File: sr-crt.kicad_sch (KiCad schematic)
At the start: 15 parts, among them J1 Conn_02x03_Odd_Even, J2 Barrel_Jack_MountingPin, U1 SN65LVDS2DBV, U2 SN65LVDS2DBV, U3 ADuM1200BR

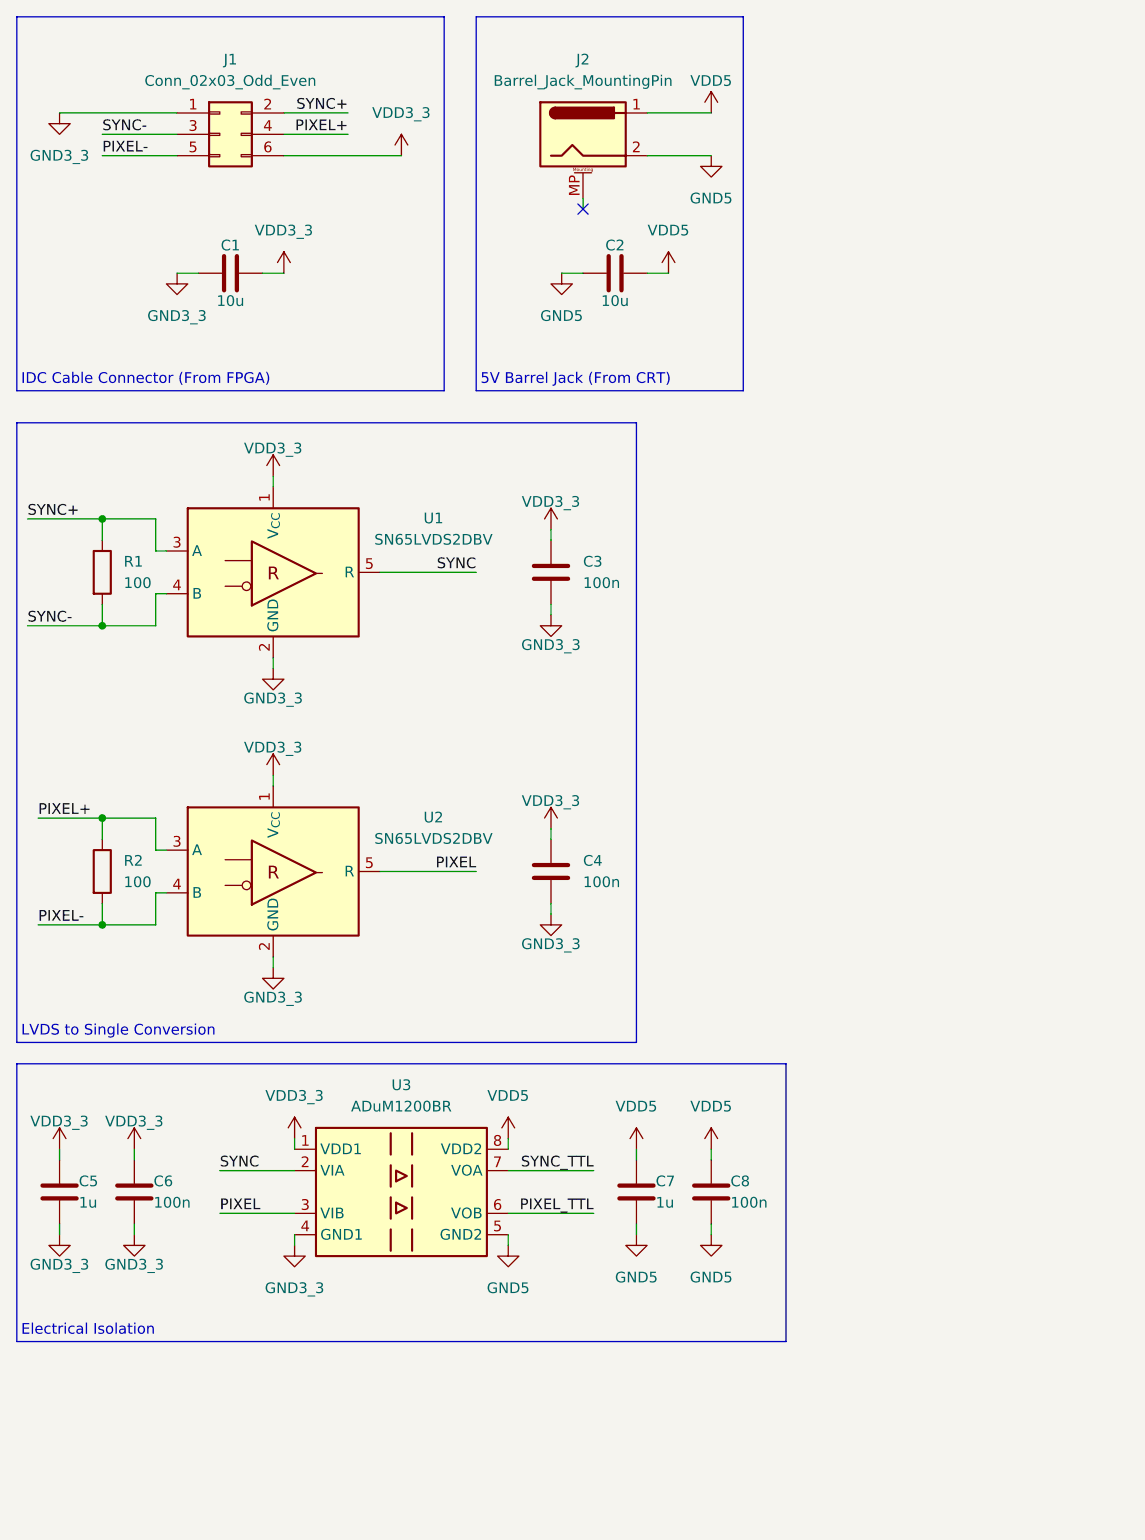
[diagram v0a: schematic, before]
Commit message: Started PCB
Also finished the schematic (as far as I am aware). Need to make DIN 6pin footprint once the connector arrives and I can measure it
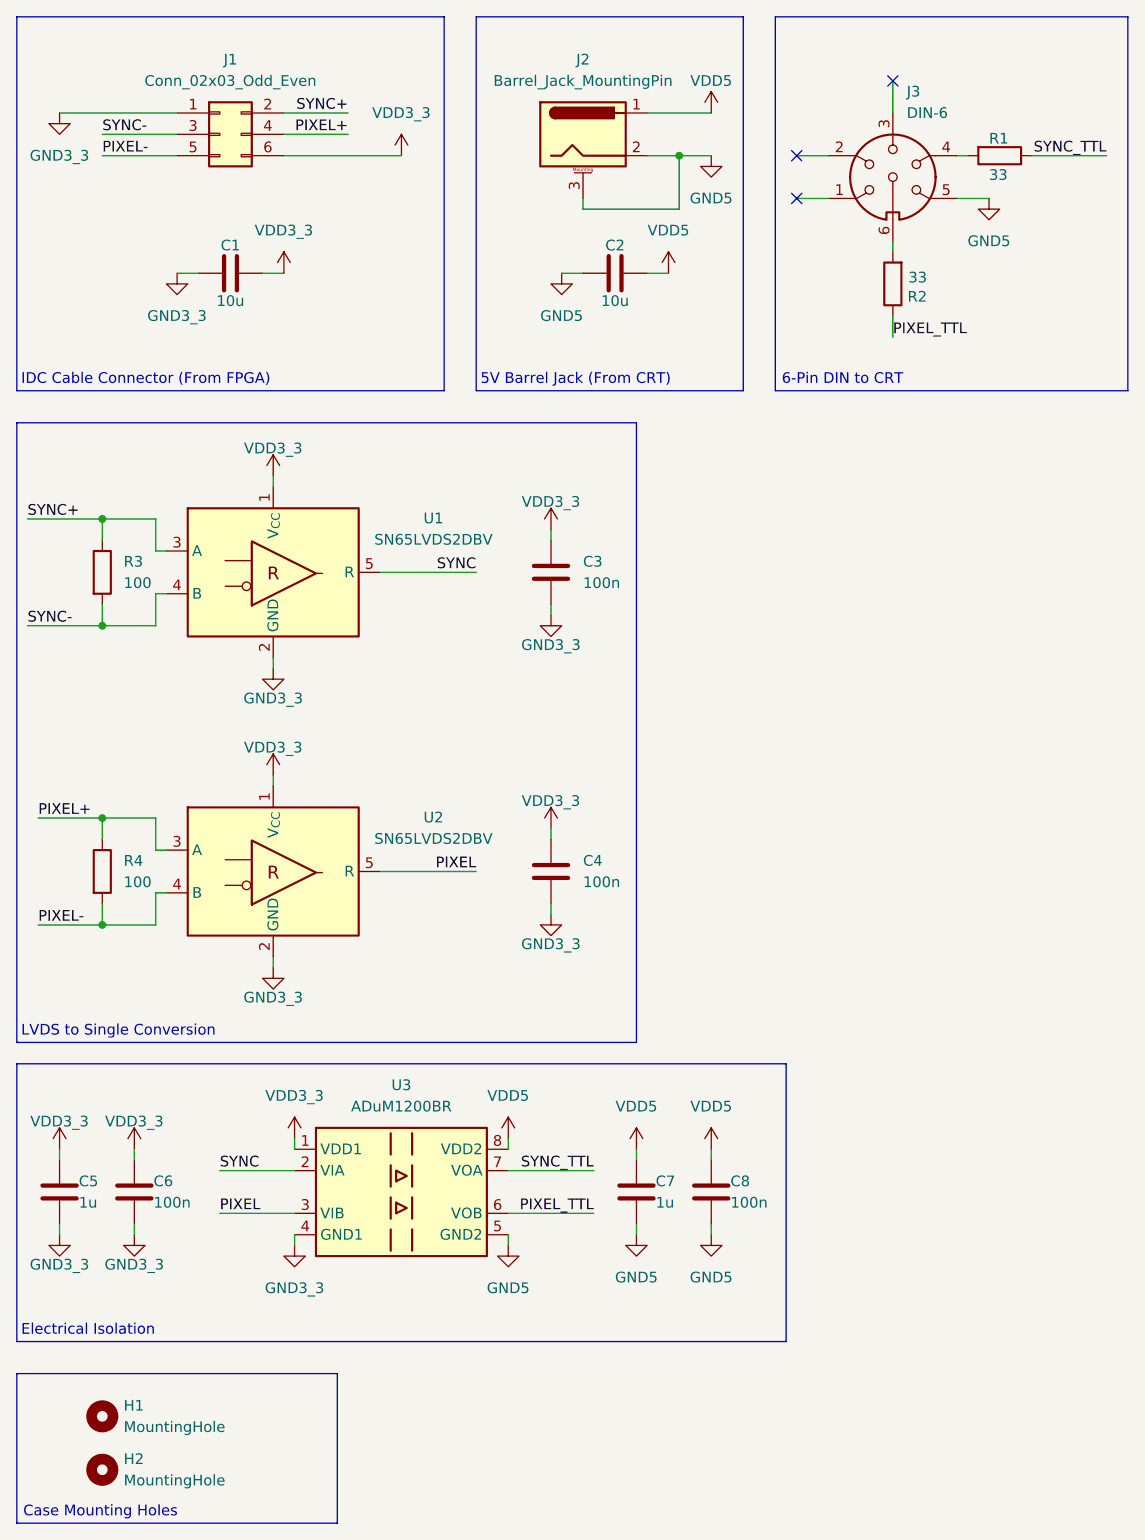
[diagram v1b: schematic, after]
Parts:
- added H1, H2: MountingHole, MountingHole:MountingHole_2.2mm_M2_ISO7380_Pad_TopBottom, symbol Mechanical:MountingHole
- added J3: DIN-6, CustomFootprints:6_PIN_DIN, symbol Connector:DIN-6
- added R1, R2: 33, Resistor_SMD:R_0603_1608Metric, symbol Device:R
- renumbered R1 to R3, R2 to R4
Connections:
- net GND5: now also J2.3 (MountPin), J3.5
- net PIXEL_TTL: now also R2.1
- net SYNC_TTL: now also R1.1
- new net: J3.4, R1.2
- new net: J3.6, R2.2
- no-connect marks 1 -> 3
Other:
- note added: "6-Pin DIN to CRT"
- note added: "Case Mounting Holes"
- company: (none) -> SRB Computer Co
- title: (none) -> SR-CRT

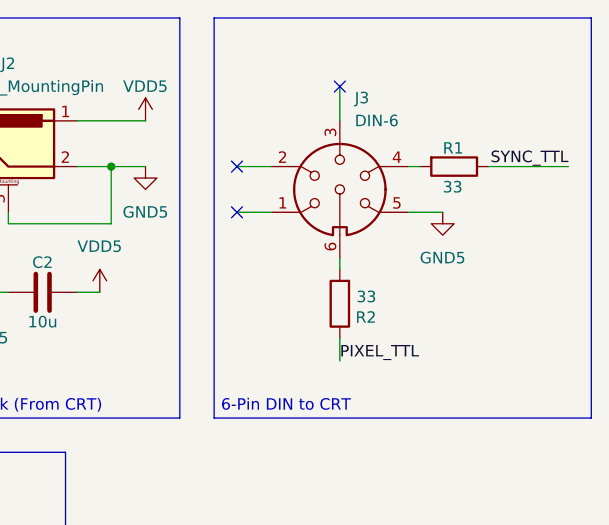
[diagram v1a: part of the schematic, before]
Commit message: Updated PCB
Fixed pin issues
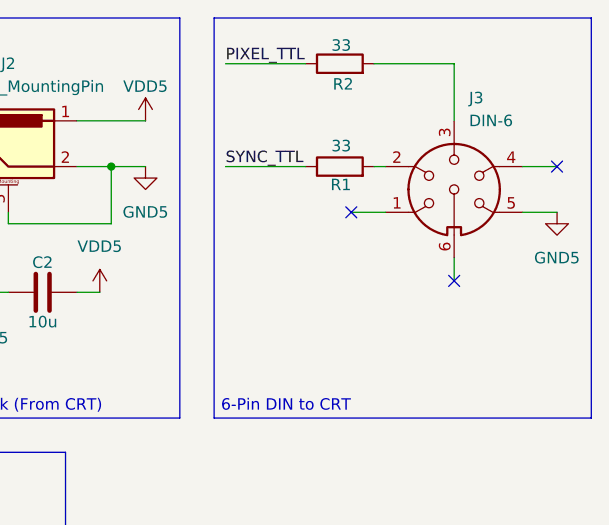
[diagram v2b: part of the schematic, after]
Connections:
- net at R1.2: now also J3.2; no longer J3.4
- net at R2.2: now also J3.3; no longer J3.6
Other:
- moved on the sheet: J3, R1, R2
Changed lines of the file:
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@@
 	)
 	(no_connect
-		(at 107.95 36.83)
+		(at 143.51 31.75)
 	)
 	(no_connect
-		(at 107.95 31.75)
+		(at 120.65 36.83)
 	)
 	(no_connect
-		(at 119.38 22.86)
+		(at 132.08 44.45)
 	)
 	(wire
@@
 	(wire
 		(pts
-			(xy 107.95 31.75) (xy 111.76 31.75)
+			(xy 90.17 31.75) (xy 93.98 31.75)
 		)
 		(stroke
@@
 	(wire
 		(pts
-			(xy 90.17 31.75) (xy 93.98 31.75)
+			(xy 120.65 36.83) (xy 124.46 36.83)
 		)
 		(stroke
@@
 	(wire
 		(pts
-			(xy 107.95 36.83) (xy 111.76 36.83)
+			(xy 44.45 45.72) (xy 46.99 45.72)
 		)
 		(stroke
@@
 	(wire
 		(pts
-			(xy 44.45 45.72) (xy 46.99 45.72)
+			(xy 46.99 29.21) (xy 54.61 29.21)
 		)
 		(stroke
@@
 	(wire
 		(pts
-			(xy 46.99 29.21) (xy 54.61 29.21)
+			(xy 25.4 120.65) (xy 25.4 123.19)
 		)
 		(stroke
@@
 	(wire
 		(pts
-			(xy 25.4 120.65) (xy 25.4 123.19)
+			(xy 123.19 31.75) (xy 124.46 31.75)
 		)
 		(stroke
@@
 	(wire
 		(pts
-			(xy 119.38 41.91) (xy 119.38 43.18)
+			(xy 132.08 20.32) (xy 123.19 20.32)
 		)
 		(stroke
@@
 	(wire
 		(pts
+			(xy 132.08 41.91) (xy 132.08 44.45)
+		)
+		(stroke
+			(width 0)
+			(type default)
+		)
+	)
+	(wire
+		(pts
 			(xy 25.4 29.21) (xy 34.29 29.21)
 		)
@@
 	(wire
 		(pts
-			(xy 135.89 31.75) (xy 144.78 31.75)
+			(xy 115.57 31.75) (xy 106.68 31.75)
 		)
 		(stroke
@@
 	(wire
 		(pts
-			(xy 119.38 22.86) (xy 119.38 26.67)
+			(xy 132.08 20.32) (xy 132.08 26.67)
 		)
 		(stroke
@@
 	(wire
 		(pts
+			(xy 139.7 31.75) (xy 143.51 31.75)
+		)
+		(stroke
+			(width 0)
+			(type default)
+		)
+	)
+	(wire
+		(pts
 			(xy 17.78 123.19) (xy 25.4 123.19)
 		)
@@
 	(wire
 		(pts
-			(xy 119.38 50.8) (xy 119.38 53.34)
+			(xy 115.57 20.32) (xy 106.68 20.32)
 		)
 		(stroke
@@
 	(wire
 		(pts
-			(xy 127 36.83) (xy 130.81 36.83)
+			(xy 139.7 36.83) (xy 143.51 36.83)
 		)
 		(stroke
@@
 	(wire
 		(pts
-			(xy 127 31.75) (xy 128.27 31.75)
-		)
-		(stroke
-			(width 0)
-			(type default)
-		)
-	)
-	(wire
-		(pts
 			(xy 39.37 152.4) (xy 48.26 152.4)
 		)
@@
 	)
 	(label "PIXEL_TTL"
-		(at 119.38 53.34 0)
+		(at 106.68 20.32 0)
 		(effects
 			(font
@@
 	)
 	(label "SYNC_TTL"
-		(at 144.78 31.75 180)
+		(at 106.68 31.75 0)
 		(effects
 			(font
 				(size 1.27 1.27)
 			)
-			(justify right bottom)
+			(justify left bottom)
 		)
 	)
@@
 	(symbol
 		(lib_id "Device:R")
-		(at 132.08 31.75 270)
+		(at 119.38 31.75 90)
 		(unit 1)
 		(exclude_from_sim no)
@@
 		(dnp no)
 		(property "Reference" "R1"
-			(at 130.81 29.718 90)
+			(at 120.65 33.782 90)
 			(effects
 				(font
@@
 		)
 		(property "Value" "33"
-			(at 130.81 34.036 90)
+			(at 120.65 29.464 90)
 			(effects
 				(font
@@
 		)
 		(property "Footprint" "Resistor_SMD:R_0603_1608Metric"
-			(at 132.08 29.972 90)
+			(at 119.38 33.528 90)
 			(effects
 				(font
@@
 		)
 		(property "Datasheet" "~"
-			(at 132.08 31.75 0)
+			(at 119.38 31.75 0)
 			(effects
 				(font
@@
 		)
 		(property "Description" "Resistor"
-			(at 132.08 31.75 0)
+			(at 119.38 31.75 0)
 			(effects
 				(font
@@
 	(symbol
 		(lib_id "power:GND")
-		(at 130.81 36.83 0)
+		(at 143.51 36.83 0)
 		(unit 1)
 		(exclude_from_sim no)
@@
 		(fields_autoplaced yes)
 		(property "Reference" "#PWR05"
-			(at 130.81 43.18 0)
+			(at 143.51 43.18 0)
 			(effects
 				(font
@@
 		)
 		(property "Value" "GND5"
-			(at 130.81 41.91 0)
+			(at 143.51 41.91 0)
 			(effects
 				(font
@@
 		)
 		(property "Footprint" ""
-			(at 130.81 36.83 0)
+			(at 143.51 36.83 0)
 			(effects
 				(font
@@
 		)
 		(property "Datasheet" ""
-			(at 130.81 36.83 0)
+			(at 143.51 36.83 0)
 			(effects
 				(font
@@
 		)
 		(property "Description" "Power symbol creates a global label with name \"GND\" , ground"
-			(at 130.81 36.83 0)
+			(at 143.51 36.83 0)
 			(effects
 				(font
@@
 	(symbol
 		(lib_id "Device:R")
-		(at 119.38 46.99 180)
+		(at 119.38 20.32 90)
 		(unit 1)
 		(exclude_from_sim no)
@@
 		(dnp no)
 		(property "Reference" "R2"
-			(at 123.444 48.514 0)
+			(at 120.904 22.606 90)
 			(effects
 				(font
@@
 		)
 		(property "Value" "33"
-			(at 123.444 46.228 0)
+			(at 120.65 18.288 90)
 			(effects
 				(font
@@
 		)
 		(property "Footprint" "Resistor_SMD:R_0603_1608Metric"
-			(at 121.158 46.99 90)
+			(at 119.38 22.098 90)
 			(effects
 				(font
@@
 		)
 		(property "Datasheet" "~"
-			(at 119.38 46.99 0)
+			(at 119.38 20.32 0)
 			(effects
 				(font
@@
 		)
 		(property "Description" "Resistor"
-			(at 119.38 46.99 0)
+			(at 119.38 20.32 0)
 			(effects
 				(font
@@
 	(symbol
 		(lib_id "Connector:DIN-6")
-		(at 119.38 34.29 0)
+		(at 132.08 34.29 0)
 		(unit 1)
 		(exclude_from_sim no)
@@
 		(fields_autoplaced yes)
 		(property "Reference" "J3"
-			(at 121.0311 24.13 0)
+			(at 133.7311 24.13 0)
 			(effects
 				(font
@@
 		)
 		(property "Value" "DIN-6"
-			(at 121.0311 26.67 0)
+			(at 133.7311 26.67 0)
 			(effects
 				(font
@@
 		)
 		(property "Footprint" "CustomFootprints:6_PIN_DIN"
-			(at 119.38 34.29 0)
+			(at 132.08 34.29 0)
 			(effects
 				(font
@@
 		)
 		(property "Datasheet" "http://www.mouser.com/ds/2/18/40_c091_abd_e-75918.pdf"
-			(at 119.38 34.29 0)
+			(at 132.08 34.29 0)
 			(effects
 				(font
@@
 		)
 		(property "Description" "6-pin DIN connector"
-			(at 119.38 34.29 0)
+			(at 132.08 34.29 0)
 			(effects
 				(font
